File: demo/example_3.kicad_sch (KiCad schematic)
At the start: 6 parts, among them U2 MIC841HYC5

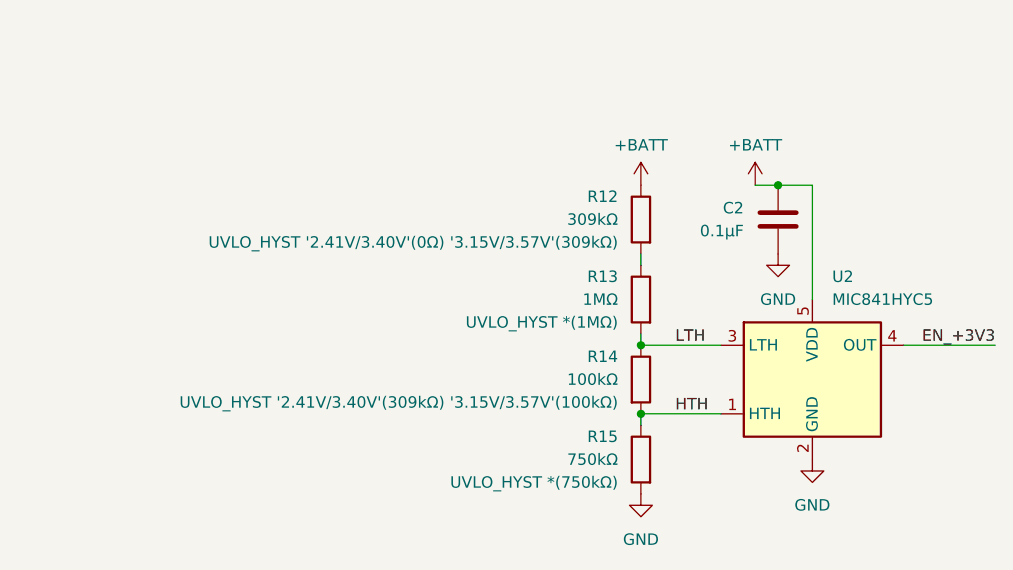
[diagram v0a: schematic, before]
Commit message: Update example project to illustrate usage of properties
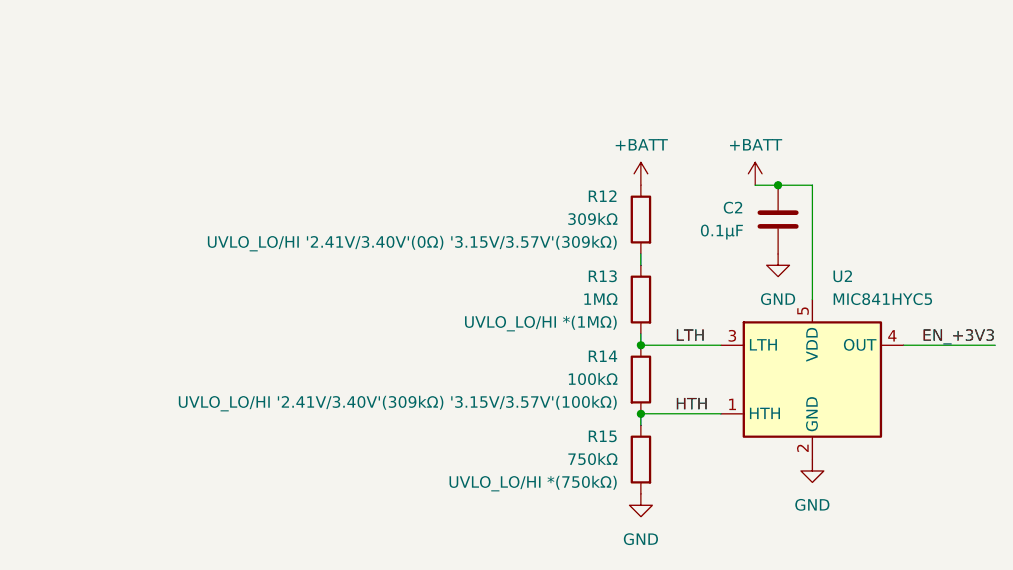
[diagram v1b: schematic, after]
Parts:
- R12: KiVar.Rule UVLO_HYST '2.41V/3.40V'(0Ω) '3.15V/3.57V'(309kΩ) -> UVLO_LO/HI '2.41V/3.40V'(0Ω) '3.15V/3.57V'(309kΩ)
- R13: KiVar.Rule UVLO_HYST *(1MΩ) -> UVLO_LO/HI *(1MΩ)
- R14: KiVar.Rule UVLO_HYST '2.41V/3.40V'(309kΩ) '3.15V/3.57V'(100kΩ) -> UVLO_LO/HI '2.41V/3.40V'(309kΩ) '3.15V/3.57V'(100kΩ)
- R15: KiVar.Rule UVLO_HYST *(750kΩ) -> UVLO_LO/HI *(750kΩ)
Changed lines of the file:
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@@
 			)
 		)
-		(property "KiVar.Rule" "UVLO_HYST '2.41V/3.40V'(309kΩ) '3.15V/3.57V'(100kΩ)"
+		(property "KiVar.Rule" "UVLO_LO/HI '2.41V/3.40V'(309kΩ) '3.15V/3.57V'(100kΩ)"
 			(at 106.045 71.1199 0)
 			(effects
@@
 			)
 		)
-		(property "KiVar.Rule" "UVLO_HYST '2.41V/3.40V'(0Ω) '3.15V/3.57V'(309kΩ)"
+		(property "KiVar.Rule" "UVLO_LO/HI '2.41V/3.40V'(0Ω) '3.15V/3.57V'(309kΩ)"
 			(at 106.045 53.3399 0)
 			(effects
@@
 			)
 		)
-		(property "KiVar.Rule" "UVLO_HYST *(750kΩ)"
+		(property "KiVar.Rule" "UVLO_LO/HI *(750kΩ)"
 			(at 106.045 80.0099 0)
 			(effects
@@
 			)
 		)
-		(property "KiVar.Rule" "UVLO_HYST *(1MΩ)"
+		(property "KiVar.Rule" "UVLO_LO/HI *(1MΩ)"
 			(at 106.045 62.2299 0)
 			(effects

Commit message: Add demo todo note
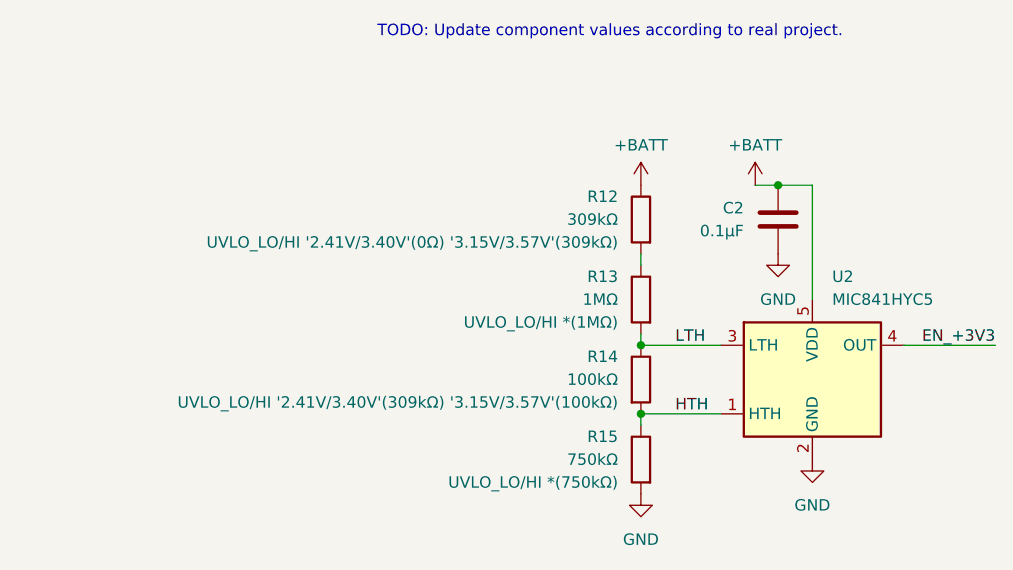
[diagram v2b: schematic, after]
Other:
- note added: "TODO: Update component values according to real project."
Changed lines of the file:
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@@
+		)
+	)
+	(text "TODO: Update component values according to real project."
+		(exclude_from_sim no)
+		(at 105.156 29.972 0)
+		(effects
+			(font
+				(size 1.27 1.27)
+			)
 		)
 	)
